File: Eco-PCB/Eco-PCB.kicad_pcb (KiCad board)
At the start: 2 copper layers, 104 x 127 mm, 16 parts, among them J1 DB25_Female, M1 SD Card, M1_1 XSOURCE Wireless, P1 Power_Block

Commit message: New PCB 1 Design with correct width for VCC & GND
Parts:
- moved P1 7.69 mm to (156.1, 25.3), turned to 270 degrees
- renumbered diode to R1
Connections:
- J1 pad 12: /GND -> Net-(J1-Pad12)
- J1 pad 13: /VCC_1 -> VCC
- J1 pad 23: Net-(J1-Pad23) -> /VCC_1
- J1 pad 25: VCC -> /GND
- Master1 pad 19: Net-(Arduino3-Pad1) -> Net-(Arduino3-Pad2)
- Master1 pad 20: Net-(Arduino3-Pad2) -> Net-(Arduino3-Pad1)
- REF** pad 1: (no net) -> /GND
- REF** pad 2: (no net) -> VCC
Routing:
- net VCC: track 0.00 -> 372.6 mm
- net /GND: track 0.00 -> 366.1 mm
- net /VCC_1: track 0.00 -> 27.0 mm
- net Net-(Arduino3-Pad2): track 0.00 -> 24.3 mm
- net Net-(Arduino3-Pad1): track 0.00 -> 24.3 mm
- net Net-(Arduino2-Pad2): track 0.00 -> 18.5 mm
- net Net-(Arduino2-Pad1): track 0.00 -> 14.0 mm
- net /OUT: track 19.2 -> 20.0 mm

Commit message: Pcb 1 design done V1.0
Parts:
- moved A2_1 14.3 mm to (149.7, 96.1), turned to 270 degrees
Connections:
- Arduino2 pad 13: Net-(Arduino2-Pad13) -> /CS
- Arduino2 pad 15: Net-(Arduino2-Pad15) -> /MISO
- Arduino2 pad 16: Net-(Arduino2-Pad16) -> /SCLK
- Arduino2 pad 23: /CS -> Net-(Arduino2-Pad23)
- Arduino2 pad 24: /MISO -> Net-(Arduino2-Pad24)
- Arduino2 pad 25: /SCLK -> Net-(Arduino2-Pad25)
- Master1 pad 12: /CS_ -> Net-(Master1-Pad12)
- Master1 pad 13: /SCK -> /CS_
- Master1 pad 16: Net-(Master1-Pad16) -> /SCK
- R1 pad 2: /SDA -> VCC
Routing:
- net VCC: track 372.6 -> 404.7 mm
- net /CS: track 30.4 -> 60.5 mm
- net /SCK: track 13.1 -> 38.0 mm
- net /MISO: track 31.5 -> 54.1 mm
- net /SCLK: track 31.4 -> 52.4 mm
- net /GND: track 366.1 -> 383.6 mm
- net /CS_: track 12.4 -> 15.7 mm

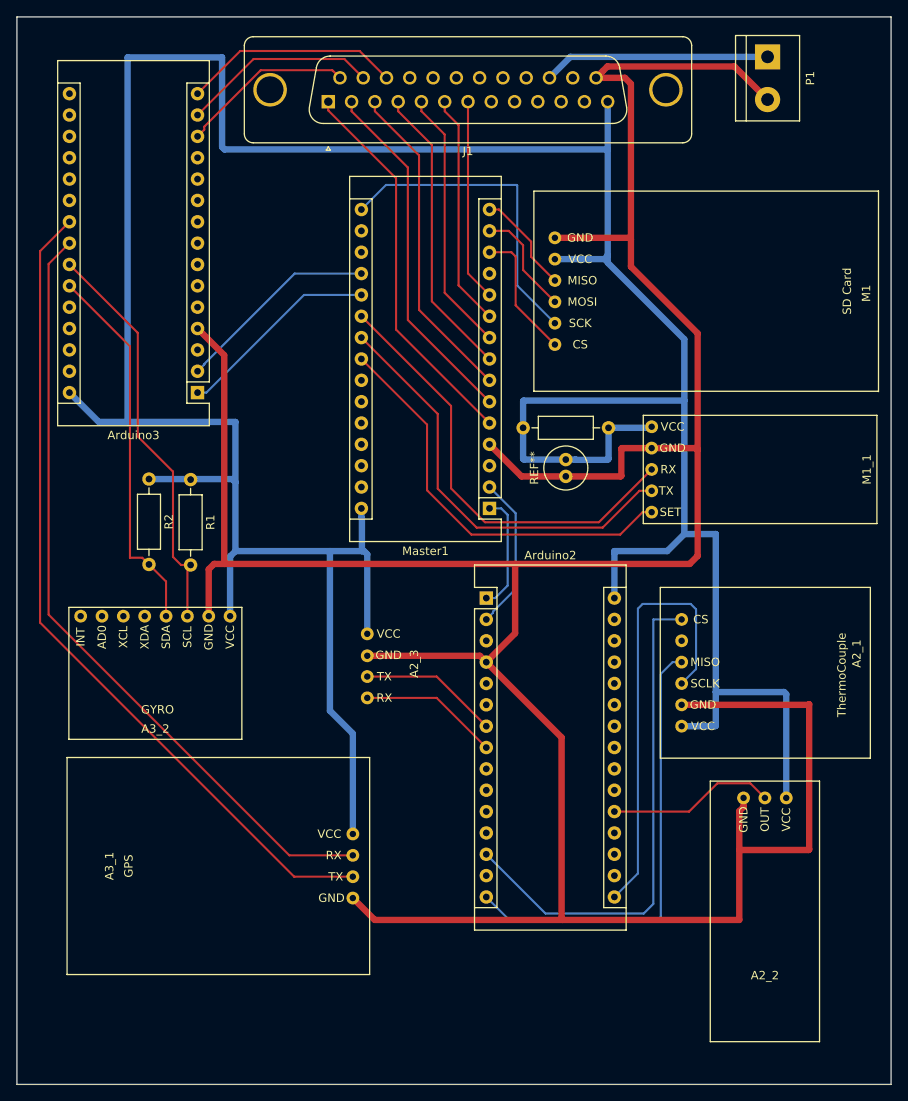
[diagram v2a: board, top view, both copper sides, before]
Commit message: PCB1 added CLK line & PCB2 Design done
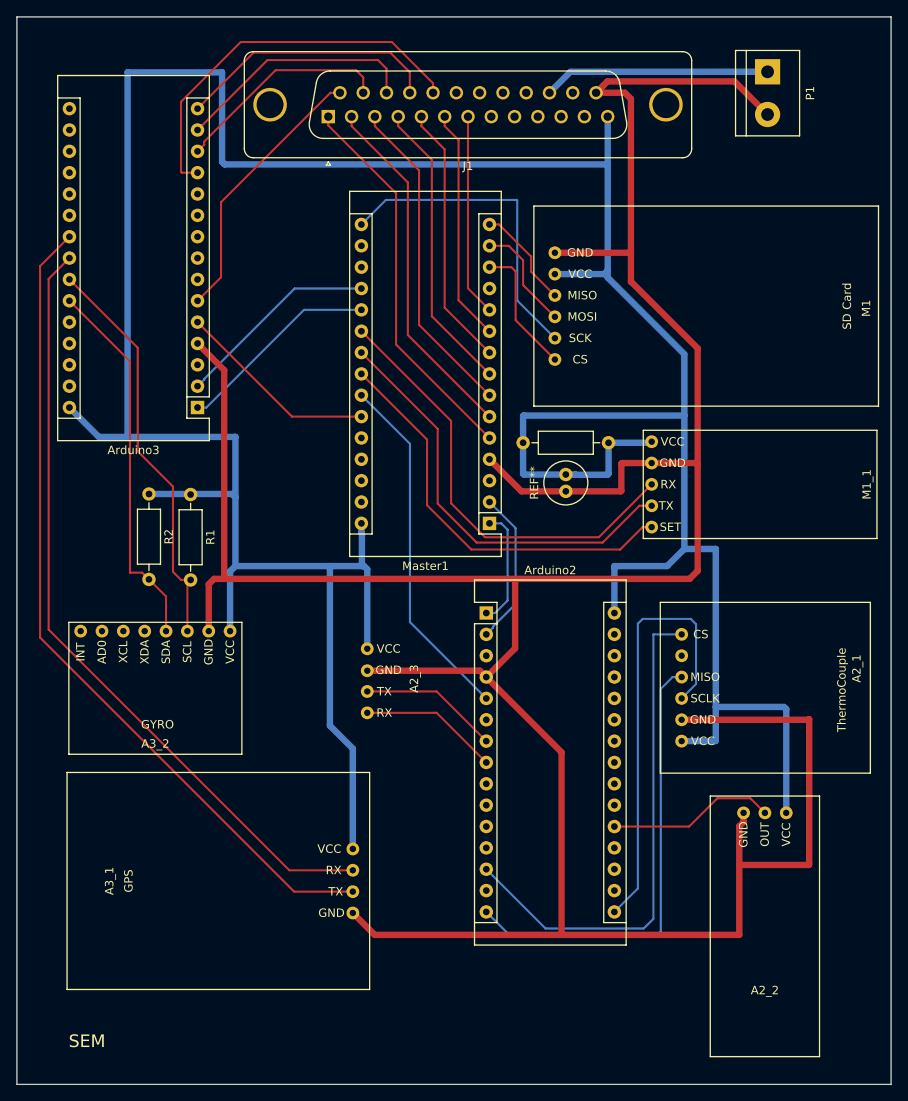
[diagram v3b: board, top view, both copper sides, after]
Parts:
- moved Arduino2 1.78 mm to (122.7, 91.5)
- moved M1_1 1.78 mm to (155.3, 76.2)
- moved R1 1.78 mm to (127.1, 71.2)
- moved R2 1.78 mm to (82.5, 77.3)
- moved J1 1.78 mm to (103.9, 32.4)
- moved M1 1.78 mm to (148.8, 55.0)
- moved P1 1.78 mm to (156.1, 27.1)
- moved A2_1 1.78 mm to (149.7, 97.9)
- moved A2_2 1.78 mm to (155.8, 128.8)
- moved A2_3 1.78 mm to (108.5, 99.6)
- moved A3_1 1.78 mm to (90.8, 123.4)
- moved A3_2 1.78 mm to (83.3, 100.5)
- moved Arduino3 1.78 mm to (88.3, 67.1)
- moved Master1 1.78 mm to (123.1, 80.8)
- moved R1 1.78 mm to (87.5, 77.4)
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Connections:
- Arduino2 pad 5: Net-(Arduino2-Pad5) -> int
- Arduino3 pad 12: Net-(Arduino3-Pad12) -> CLK3
- Arduino3 pad 13: Net-(Arduino3-Pad13) -> CLK2
- Arduino3 pad 14: Net-(Arduino3-Pad14) -> DT
- Arduino3 pad 15: Net-(Arduino3-Pad15) -> D5
- Arduino3 pad 5: Net-(Arduino3-Pad5) -> int2
- Arduino3 pad 6: Net-(Arduino3-Pad6) -> SW
- J1 pad 14: Net-(Arduino3-Pad13) -> SW
- J1 pad 15: Net-(Arduino3-Pad14) -> CLK2
- J1 pad 16: Net-(Arduino3-Pad15) -> DT
- J1 pad 17: Net-(J1-Pad17) -> D5
- J1 pad 18: Net-(J1-Pad18) -> CLK3
- Master1 pad 24: Net-(Master1-Pad24) -> int
- Master1 pad 25: Net-(Master1-Pad25) -> int2
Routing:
- net CLK3: track 0.00 -> 46.4 mm
- net int: track 0.00 -> 42.2 mm
- net SW: track 0.00 -> 32.4 mm
- net D5: track 0.00 -> 31.4 mm
- net DT: track 0.00 -> 29.2 mm
- net CLK2: track 0.00 -> 26.1 mm
- net Net-(Arduino3-Pad15): track 25.9 -> 0.00 mm
- net int2: track 0.00 -> 24.2 mm
- net Net-(Arduino3-Pad14): track 23.4 -> 0.00 mm
- net Net-(Arduino3-Pad13): track 20.8 -> 0.00 mm
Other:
- board text added: "SEM"
